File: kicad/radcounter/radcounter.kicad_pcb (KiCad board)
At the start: 2 copper layers, 11.2 x 8.4 mm, 34 parts, among them J1 SiPM(+), J2 SiPM(-), J3 Out, J4 Conn, J5 Conn, J6 Conn, Q2 RUM002N05T2L, T1 ATB322515-0110-T000, U2 MAX9120EXK

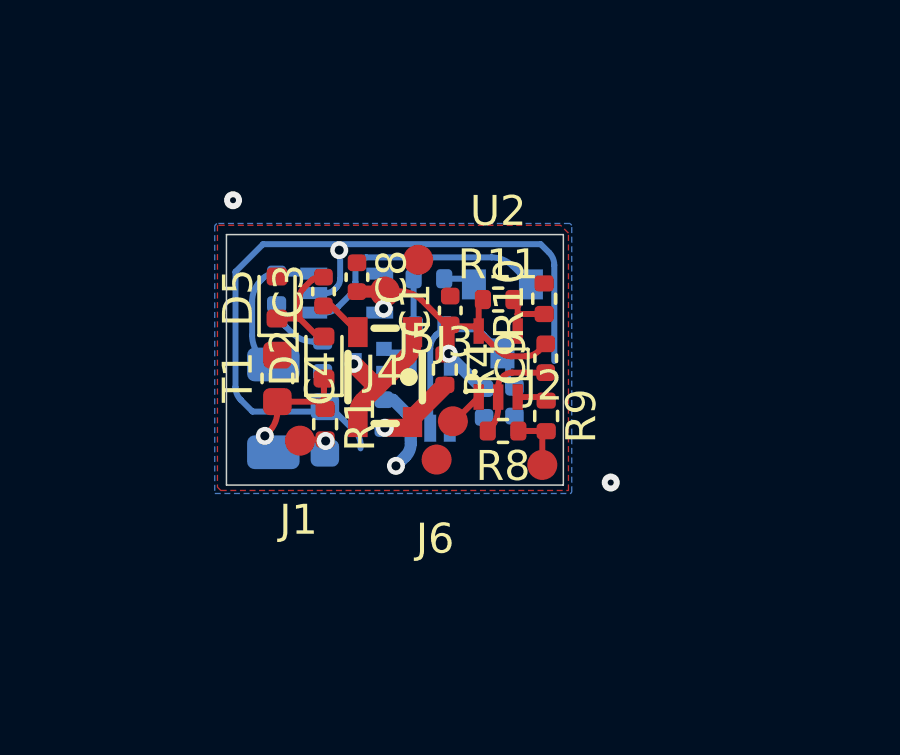
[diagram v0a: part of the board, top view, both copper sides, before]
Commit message: удалено:       kicad/radcounter/radcounter-backups/radcounter-2025-12-29_170945.zip 	изменено:      kicad/radcounter/radcounter.kicad_pcb
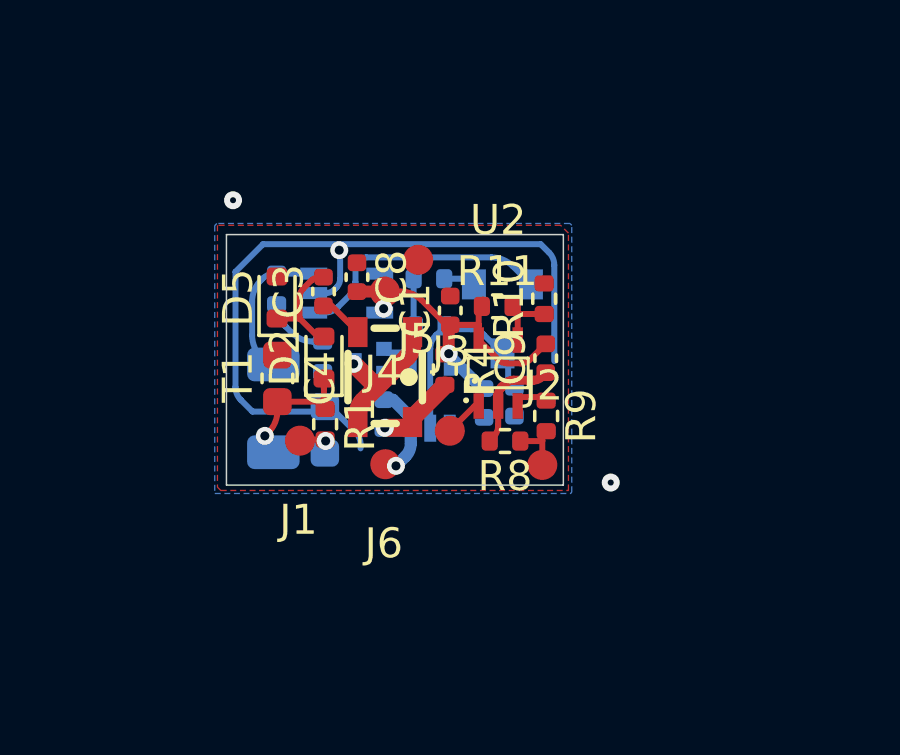
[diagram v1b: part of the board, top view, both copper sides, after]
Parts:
- moved J6 1.72 mm to (112.9, 52.2)
- moved R8 0.34 mm to (116.9, 51.4)
- moved J3 0.33 mm to (115.1, 51.1)
- moved U2 0.30 mm to (116.7, 49.2)
- moved R11 0.23 mm to (116.6, 46.9)
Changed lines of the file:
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@@
 	(footprint "lib:ConnMini"
 		(layer "F.Cu")
-		(at 115.167746 50.774374 180)
+		(at 115.065545 51.089194 180)
 		(property "Reference" "J3"
 			(at -0.05 2.64 180)
@@
 	(footprint "lib:ConnMini"
 		(layer "F.Cu")
-		(at 114.625201 52.05)
+		(at 112.915928 52.204409)
 		(property "Reference" "J6"
 			(at -0.05 2.64 0)
@@
 	(footprint "Resistor_SMD:R_0402_1005Metric"
 		(layer "F.Cu")
-		(at 116.839469 51.096028 180)
+		(at 116.904931 51.432648 180)
 		(descr "Resistor SMD 0402 (1005 Metric), square (rectangular) end terminal, IPC-7351 nominal, (Body size source: IPC-SM-782 page 72, https://www.pcb-3d.com/wordpress/wp-content/uploads/ipc-sm-782a_amendment_1_and_2.pdf), generated with kicad-footprint-generator")
 		(tags "resistor")
@@
 	(footprint "easyeda2kicad:SC-70-5_L2.0-W1.3-P0.65-LS2.1-BL"
 		(layer "F.Cu")
-		(at 116.677843 48.865598)
+		(at 116.677843 49.165404)
 		(property "Reference" "U2"
 			(at 0 -5.1 0)
@@
 		(model "${EASYEDA2KICAD}/easyeda2kicad.3dshapes/SC-70-5_L2.0-W1.3-P0.65-LS2.1-BL.wrl"
 			(offset
-				(xyz -0 0 -0)
+				(xyz -0 0 0.5)
 			)
 			(scale
@@
 			)
 			(rotate
-				(xyz 0 0 0)
+				(xyz -0 -0 -0)
 			)
 		)
@@
 	(footprint "Resistor_SMD:R_0402_1005Metric"
 		(layer "F.Cu")
-		(at 116.677843 46.715981)
+		(at 116.645162 46.943105)
 		(descr "Resistor SMD 0402 (1005 Metric), square (rectangular) end terminal, IPC-7351 nominal, (Body size source: IPC-SM-782 page 72, https://www.pcb-3d.com/wordpress/wp-content/uploads/ipc-sm-782a_amendment_1_and_2.pdf), generated with kicad-footprint-generator")
 		(tags "resistor")
@@
 	)
 	(segment
-		(start 116.677843 49.611653)
-		(end 116.677843 49.965598)
+		(start 116.677843 50.265404)
+		(end 116.677843 50.901208)
 		(width 0.2)
 		(layer "F.Cu")
@@
 	(segment
 		(start 118.261772 49.151648)
-		(end 117.137848 49.151648)
-		(width 0.2)
+		(end 118.126573 49.286847)
+		(width 0.3)
 		(layer "F.Cu")
 		(net 1)
 	)
 	(segment
-		(start 116.677843 49.965598)
-		(end 116.677843 50.33344)
-		(width 0.2)
+		(start 116.677843 49.91206)
+		(end 116.677843 50.265404)
+		(width 0.3)
 		(layer "F.Cu")
 		(net 1)
 	)
 	(segment
-		(start 116.855005 49.268806)
-		(end 116.795 49.328811)
+		(start 116.502107 51.325472)
+		(end 116.394931 51.432648)
 		(width 0.2)
 		(layer "F.Cu")
@@
 	)
 	(segment
-		(start 116.38495 51.040547)
-		(end 116.329469 51.096028)
-		(width 0.2)
+		(start 117.843731 49.404004)
+		(end 117.185899 49.404004)
+		(width 0.3)
+		(layer "F.Cu")
+		(net 1)
+	)
+	(segment
+		(start 116.903056 49.521162)
+		(end 116.795 49.629218)
+		(width 0.3)
 		(layer "F.Cu")
 		(net 1)
@@
 	)
 	(arc
-		(start 117.137848 49.151648)
-		(mid 116.984774 49.182096)
-		(end 116.855005 49.268806)
+		(start 116.677843 50.901208)
+		(mid 116.632171 51.130818)
+		(end 116.502107 51.325472)
 		(width 0.2)
 		(layer "F.Cu")
@@
 	)
 	(arc
-		(start 116.677843 49.611653)
-		(mid 116.708291 49.45858)
-		(end 116.795 49.328811)
-		(width 0.2)
+		(start 117.843731 49.404004)
+		(mid 117.996804 49.373556)
+		(end 118.126573 49.286847)
+		(width 0.3)
 		(layer "F.Cu")
 		(net 1)
 	)
 	(arc
-		(start 116.38495 51.040547)
-		(mid 116.601723 50.716124)
-		(end 116.677843 50.33344)
-		(width 0.2)
+		(start 116.677843 49.91206)
+		(mid 116.708291 49.758987)
+		(end 116.795 49.629218)
+		(width 0.3)
+		(layer "F.Cu")
+		(net 1)
+	)
+	(arc
+		(start 117.185899 49.404004)
+		(mid 117.032825 49.434452)
+		(end 116.903056 49.521162)
+		(width 0.3)
 		(layer "F.Cu")
 		(net 1)
@@
 	)
 	(segment
+		(start 118.261619 48.191648)
+		(end 118.261772 48.191648)
+		(width 0.2)
+		(layer "F.Cu")
+		(net 2)
+	)
+	(segment
 		(start 115.03 48.52)
 		(end 115.03 47.61)
@@
 	)
 	(segment
+		(start 116.970484 48.84236)
+		(end 117.445222 48.84236)
+		(width 0.2)
+		(layer "F.Cu")
+		(net 2)
+	)
+	(segment
 		(start 114.97 48.47)
 		(end 114.97 48.35)
@@
 	)
 	(segment
-		(start 118.022158 48.431262)
-		(end 118.261772 48.191648)
+		(start 117.728065 48.725202)
+		(end 118.261619 48.191648)
 		(width 0.2)
 		(layer "F.Cu")
@@
 	)
 	(segment
-		(start 116.027843 47.765598)
-		(end 116.693507 48.431262)
+		(start 115.08 47.56)
+		(end 116.027419 47.56)
 		(width 0.2)
 		(layer "F.Cu")
@@
 	)
 	(segment
-		(start 116.027843 47.765598)
+		(start 116.027843 47.560424)
 		(end 116.027843 46.855981)
 		(width 0.2)
@@
 	(segment
 		(start 115.03 47.61)
-		(end 115.872245 47.61)
-		(width 0.2)
-		(layer "F.Cu")
-		(net 2)
-	)
-	(segment
-		(start 115.03 47.61)
 		(end 115.08 47.56)
 		(width 0.2)
@@
 	)
 	(segment
-		(start 115.872245 47.61)
-		(end 116.027843 47.765598)
+		(start 115.04 47.67)
+		(end 115.15 47.67)
 		(width 0.2)
 		(layer "F.Cu")
@@
 	)
 	(segment
-		(start 117.117771 48.606998)
-		(end 117.597894 48.606998)
+		(start 116.027843 47.765598)
+		(end 116.027843 47.560424)
 		(width 0.2)
 		(layer "F.Cu")
@@
 	)
 	(segment
-		(start 115.04 47.67)
-		(end 115.15 47.67)
+		(start 116.027419 47.56)
+		(end 116.027843 47.560424)
+		(width 0.2)
+		(layer "F.Cu")
+		(net 2)
+	)
+	(segment
+		(start 116.027843 48.065404)
+		(end 116.687642 48.725203)
 		(width 0.2)
 		(layer "F.Cu")
@@
 	)
 	(arc
-		(start 117.117771 48.606998)
-		(mid 116.888161 48.561326)
-		(end 116.693507 48.431262)
+		(start 117.728065 48.725202)
+		(mid 117.598296 48.811911)
+		(end 117.445222 48.84236)
 		(width 0.2)
 		(layer "F.Cu")
@@
 	)
 	(arc
-		(start 114.132893 46.742893)
-		(mid 113.80847 46.52612)
-		(end 113.425786 46.45)
+		(start 116.970484 48.84236)
+		(mid 116.817411 48.811912)
+		(end 116.687642 48.725203)
 		(width 0.2)
 		(layer "F.Cu")
@@
 	)
 	(arc
-		(start 118.022158 48.431262)
-		(mid 117.827504 48.561326)
-		(end 117.597894 48.606998)
+		(start 114.132893 46.742893)
+		(mid 113.80847 46.52612)
+		(end 113.425786 46.45)
 		(width 0.2)
 		(layer "F.Cu")
@@
 	)
 	(segment
-		(start 118.148634 52.227405)
+		(start 117.414931 51.432648)
+		(end 118.13741 51.432648)
+		(width 0.2)
+		(layer "F.Cu")
+		(net 11)
+	)
+	(segment
+		(start 118.148634 51.421424)
 		(end 118.148634 51.234289)
 		(width 0.2)
@@
 	)
 	(segment
-		(start 117.349469 51.096028)
-		(end 118.268973 51.096028)
+		(start 118.148634 52.227405)
+		(end 118.148634 51.421424)
 		(width 0.2)
 		(layer "F.Cu")
@@
 	)
 	(segment
-		(start 115.271703 50.721738)
-		(end 116.027843 49.965598)
+		(start 118.13741 51.432648)
+		(end 118.148634 51.421424)
+		(width 0.2)
+		(layer "F.Cu")
+		(net 11)
+	)
+	(segment
+		(start 116.027843 50.265404)
+		(end 115.889335 50.265404)
 		(width 0.2)
 		(layer "F.Cu")
@@
 	)
 	(segment
-		(start 115.271703 50.85359)
-		(end 115.271703 50.721738)
+		(start 115.889335 50.265404)
+		(end 115.065545 51.089194)
 		(width 0.2)
 		(layer "F.Cu")

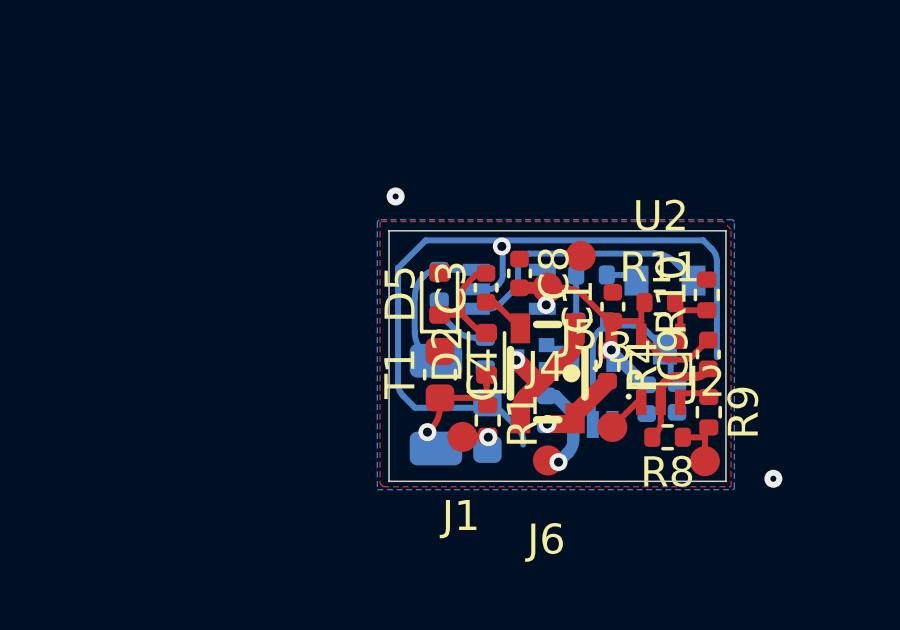
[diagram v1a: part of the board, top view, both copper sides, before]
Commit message: удалено:       kicad/radcounter/radcounter-backups/radcounter-2025-12-29_171823.zip 	удалено:       kicad/radcounter/radcounter-backups/radcounter-2026-01-03_121429.zip 	изменено:      kicad/radcounter/radcounter.kicad_pcb 	изменено:      kicad/radcounter/radcounter.kicad_prl 	изменено:      kicad/radcounter/radcounter.kicad_sch
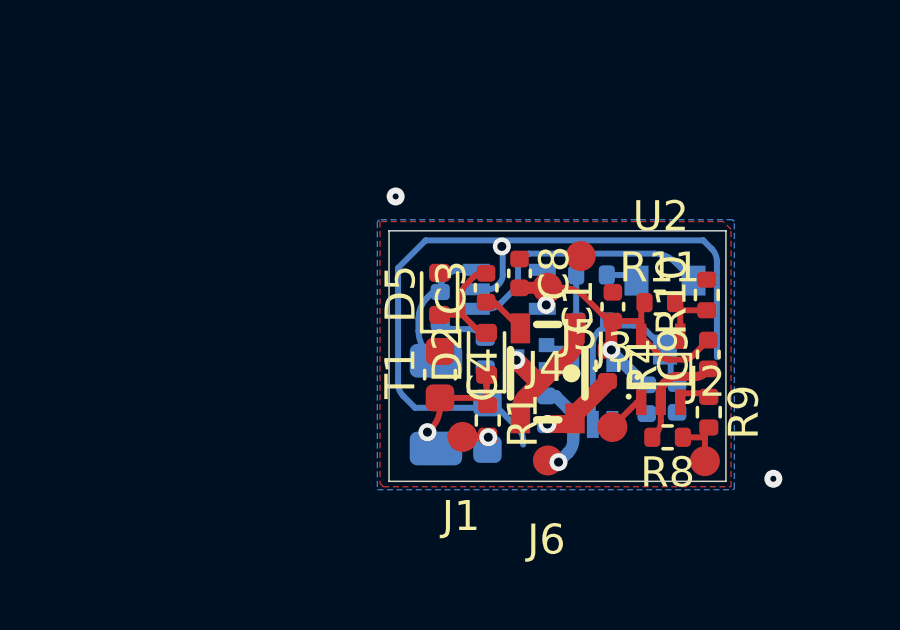
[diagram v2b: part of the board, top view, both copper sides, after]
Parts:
- moved R5 0.74 mm to (109.3, 47.1)
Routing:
- net Net-(D3-+): track 5.10 -> 4.52 mm
- net Net-(R5-Pad2): track 2.21 -> 1.65 mm
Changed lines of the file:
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@@
 	(footprint "Resistor_SMD:R_0402_1005Metric"
 		(layer "B.Cu")
-		(at 109.291674 46.362893 -90)
+		(at 109.327577 47.098592 -90)
 		(descr "Resistor SMD 0402 (1005 Metric), square (rectangular) end terminal, IPC-7351 nominal, (Body size source: IPC-SM-782 page 72, https://www.pcb-3d.com/wordpress/wp-content/uploads/ipc-sm-782a_amendment_1_and_2.pdf), generated with kicad-footprint-generator")
 		(tags "resistor")
@@
 	)
 	(segment
-		(start 108.476813 46.778229)
-		(end 108.476813 47.913774)
+		(start 108.602435 47.482407)
+		(end 108.602435 47.885338)
 		(width 0.2)
 		(layer "B.Cu")
@@
 	(segment
 		(start 110.53 45.85)
-		(end 109.294567 45.85)
+		(end 109.984717 45.85)
 		(width 0.2)
 		(layer "B.Cu")
@@
 	)
 	(segment
-		(start 109.294567 45.85)
-		(end 109.291674 45.852893)
+		(start 109.327577 46.50714)
+		(end 109.327577 46.588592)
 		(width 0.2)
 		(layer "B.Cu")
@@
 	)
 	(segment
-		(start 108.812199 46.028629)
-		(end 108.769706 46.071122)
+		(start 109.560453 46.025736)
+		(end 109.503313 46.082876)
 		(width 0.2)
 		(layer "B.Cu")
@@
 	)
 	(segment
-		(start 108.769706 48.620881)
-		(end 109.177788 49.028963)
+		(start 108.895328 48.592445)
+		(end 109.182988 48.880105)
 		(width 0.2)
 		(layer "B.Cu")
@@
 	)
 	(segment
-		(start 109.291674 45.852893)
-		(end 109.236463 45.852893)
+		(start 109.327577 46.588592)
+		(end 109.082036 46.588592)
+		(width 0.2)
+		(layer "B.Cu")
+		(net 6)
+	)
+	(segment
+		(start 109.082036 46.588592)
+		(end 108.895328 46.7753)
+		(width 0.2)
+		(layer "B.Cu")
+		(net 6)
+	)
+	(arc
+		(start 108.602435 47.482407)
+		(mid 108.678555 47.099724)
+		(end 108.895328 46.7753)
 		(width 0.2)
 		(layer "B.Cu")
@@
 	)
 	(arc
-		(start 108.769706 48.620881)
-		(mid 108.552933 48.296458)
-		(end 108.476813 47.913774)
+		(start 109.984717 45.85)
+		(mid 109.755107 45.895672)
+		(end 109.560453 46.025736)
 		(width 0.2)
 		(layer "B.Cu")
@@
 	)
 	(arc
-		(start 108.476813 46.778229)
-		(mid 108.552933 46.395546)
-		(end 108.769706 46.071122)
+		(start 108.602435 47.885338)
+		(mid 108.678555 48.268021)
+		(end 108.895328 48.592445)
 		(width 0.2)
 		(layer "B.Cu")
@@
 	)
 	(arc
-		(start 109.236463 45.852893)
-		(mid 109.006853 45.898565)
-		(end 108.812199 46.028629)
+		(start 109.327577 46.50714)
+		(mid 109.373249 46.27753)
+		(end 109.503313 46.082876)
 		(width 0.2)
 		(layer "B.Cu")
@@
 	)
 	(segment
-		(start 110.507972 48.115648)
-		(end 110.827115 48.115648)
+		(start 109.327577 47.608592)
+		(end 109.371399 47.652414)
 		(width 0.2)
 		(layer "B.Cu")
@@
 	)
 	(segment
-		(start 109.584567 47.606457)
-		(end 109.800865 47.822755)
+		(start 109.795663 47.82815)
+		(end 110.291089 47.82815)
 		(width 0.2)
 		(layer "B.Cu")
@@
 	)
 	(segment
-		(start 109.291674 46.872893)
-		(end 109.291674 46.89935)
+		(start 110.715353 48.003886)
+		(end 110.827115 48.115648)
 		(width 0.2)
 		(layer "B.Cu")
@@
 	)
 	(arc
-		(start 109.800865 47.822755)
-		(mid 110.125288 48.039528)
-		(end 110.507972 48.115648)
+		(start 109.795663 47.82815)
+		(mid 109.566053 47.782478)
+		(end 109.371399 47.652414)
 		(width 0.2)
 		(layer "B.Cu")
@@
 	)
 	(arc
-		(start 109.584567 47.606457)
-		(mid 109.367794 47.282034)
-		(end 109.291674 46.89935)
+		(start 110.715353 48.003886)
+		(mid 110.520699 47.873822)
+		(end 110.291089 47.82815)
 		(width 0.2)
 		(layer "B.Cu")

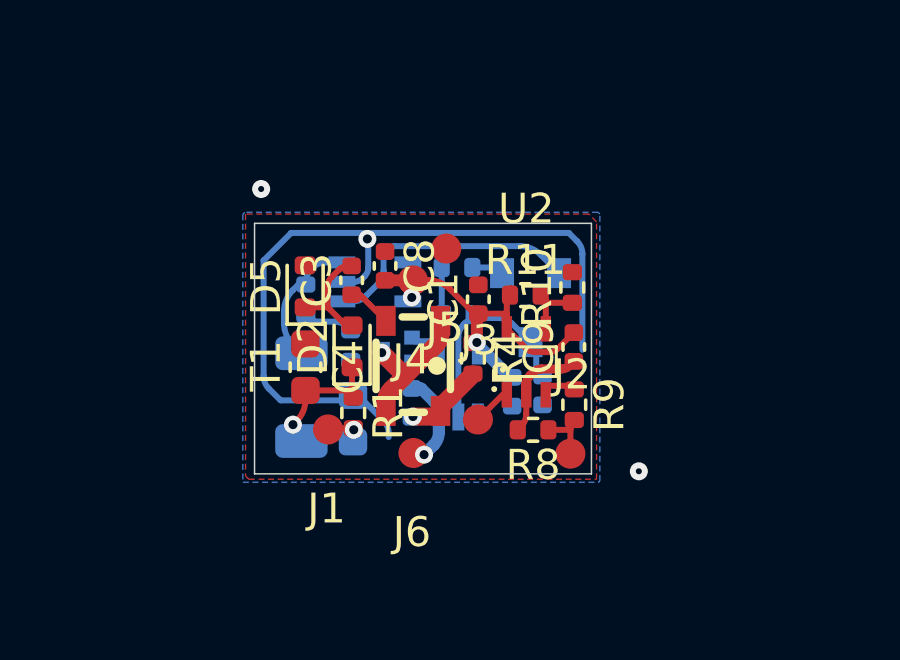
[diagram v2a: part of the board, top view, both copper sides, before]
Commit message: новый файл:    Documents/16x80-2.png 	новый файл:    Documents/not-load.png 	изменено:      kicad/radcounter/gerber/radcounter.drl 	удалено:       kicad/radcounter/gerber/radcounter_T01_0.20mm.gcode 	удалено:       kicad/radcounter/gerber/radcounter_T02_0.30mm.gcode 	удалено:       kicad/radcounter/radcounter-backups/radcounter-2026-01-03_122439.zip 	удалено:       kicad/radcounter/radcounter-backups/radcounter-2026-01-03_123621.zip 	изменено:      kicad/radcounter/radcounter.kicad_pcb
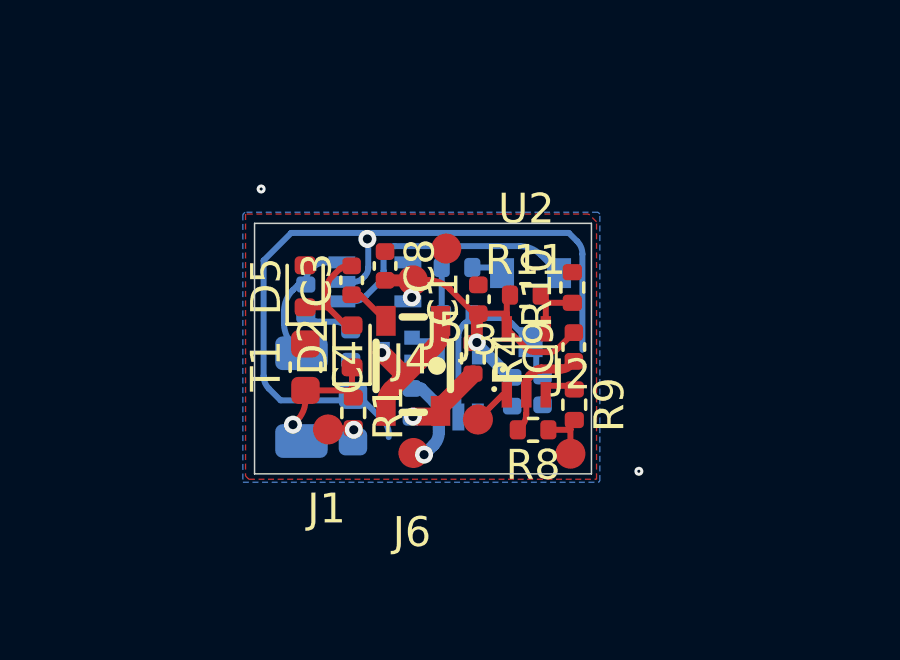
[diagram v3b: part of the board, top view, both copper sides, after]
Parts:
- R10: value 82k -> 240k
- R11: value 10M -> 30M
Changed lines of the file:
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@@
 			)
 		)
-		(property "Value" "82k"
+		(property "Value" "240k"
 			(at 0 1.17 90)
 			(layer "F.Fab")
@@
 			)
 		)
-		(property "Value" "10M"
+		(property "Value" "30M"
 			(at 0 1.17 0)
 			(layer "F.Fab")
@@
 	(via
 		(at 120.43 52.815)
-		(size 0.6)
-		(drill 0.2)
+		(size 0.3)
+		(drill 0.1)
 		(layers "F.Cu" "B.Cu")
 		(net 0)
@@
 	(via
 		(at 107.84 43.405)
-		(size 0.6)
-		(drill 0.2)
+		(size 0.3)
+		(drill 0.1)
 		(layers "F.Cu" "B.Cu")
 		(net 0)
